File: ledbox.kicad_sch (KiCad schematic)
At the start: 0 parts

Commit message: Added XIAO
ledbox.kicad_pro: me changed 1 ERC rule severity; changed schematic
  settings.
ledbox.kicad_sch: me added U1 (XIAO-ESP32-C6-SMD).
pcbjam.lock.json: Library lockfile regenerated.

Checks: ERC: 19 errors in ledbox.kicad_sch (pin not connected ×18, power pin not driven ×1)

PCBJam-Commit: 692f007c-0890-4559-b9f4-d7b86e191ada
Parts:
- added U1: XIAO-ESP32-C6-SMD, Seeed_Studio_XIAO_Series:XIAO-ESP32-C6-SMD, symbol Seeed_Studio_XIAO_Series:XIAO-ESP32-C6-SMD
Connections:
- new net +3V3: U1.12 (3V3_OUT)
- new net +5V: U1.14 (VBUS)
- new net GND: U1.13 (GND), U1.24 (GND)
- no-connect marks 0 -> 2

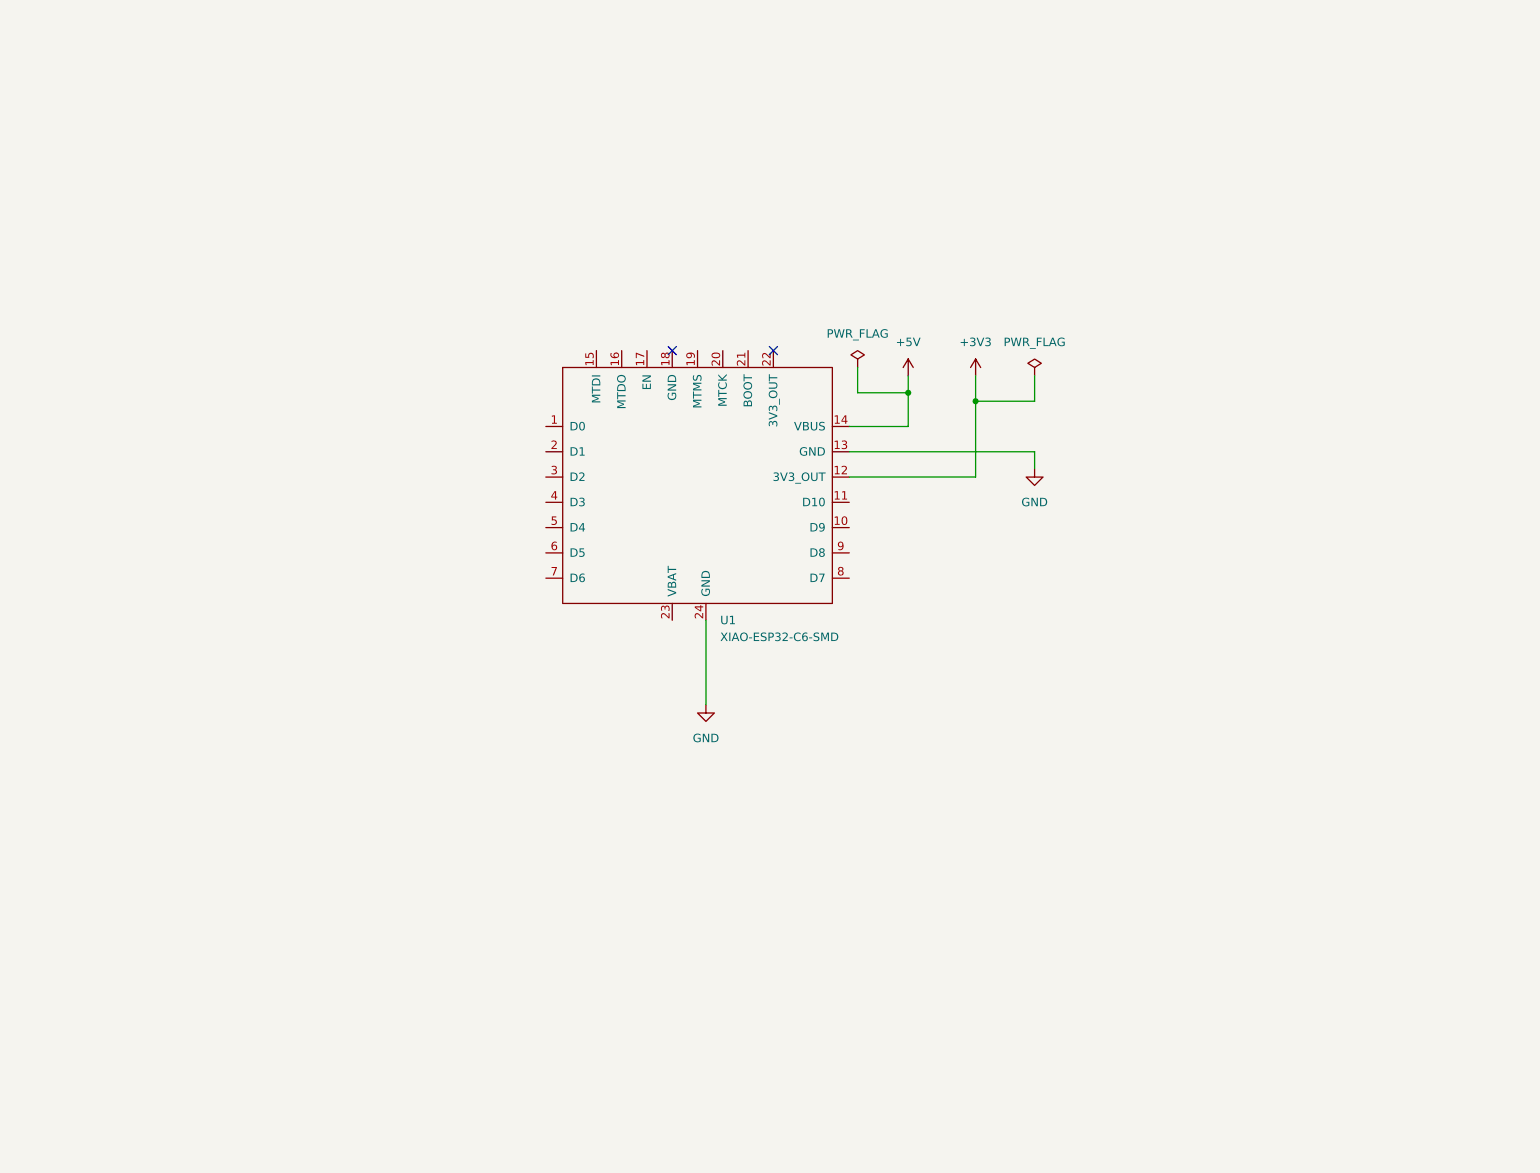
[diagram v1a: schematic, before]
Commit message: Finished Schematic.
ledbox.kicad_pro: me changed schematic settings.
ledbox.kicad_sch: me added D1, D2, J1-J8, SW1, SW2, TP1-TP4 and U2 and
  wired them; renamed net unconnected-(U1-D8-Pad9) to /A8; renamed net
  unconnected-(U1-D10-Pad11) to /STATUS_LED; rearranged the sheet around
  U1.
pcbjam.lock.json: Library lockfile regenerated.

Checks: ERC: 3 errors in ledbox.kicad_sch (pin not connected ×2, power pin not driven ×1)

PCBJam-Commit: e7df7650-f565-49c5-9b0e-8d383a5cb507
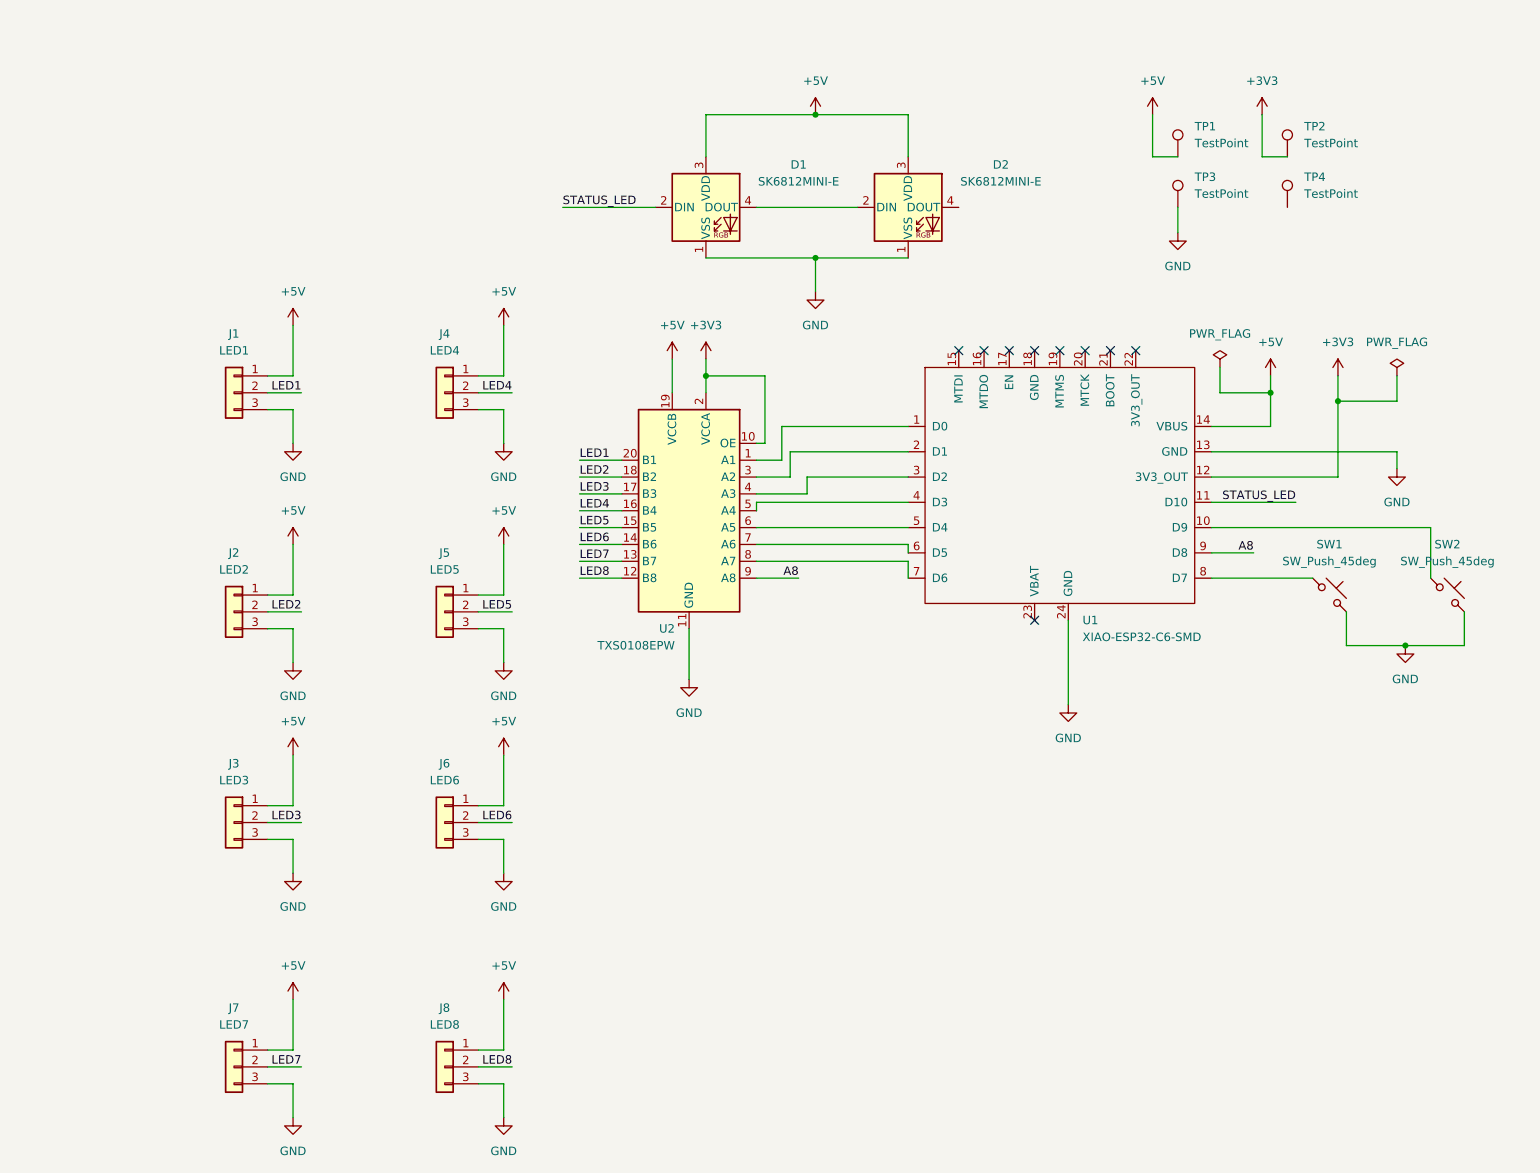
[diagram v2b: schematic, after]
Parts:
- added D1, D2: SK6812MINI-E, LED_SMD:LED_SK6812MINI-E_3.2x2.8mm_P1.5mm_ReverseMount, symbol LED:SK6812MINI-E
- added J1: LED1, symbol Connector_Generic:Conn_01x03
- added J2: LED2, symbol Connector_Generic:Conn_01x03
- added J3: LED3, symbol Connector_Generic:Conn_01x03
- added J4: LED4, symbol Connector_Generic:Conn_01x03
- added J5: LED5, symbol Connector_Generic:Conn_01x03
- added J6: LED6, symbol Connector_Generic:Conn_01x03
- added J7: LED7, symbol Connector_Generic:Conn_01x03
- added J8: LED8, symbol Connector_Generic:Conn_01x03
- added SW1, SW2: SW_Push_45deg, symbol Switch:SW_Push_45deg
- added TP1, TP2, TP3, TP4: TestPoint, TestPoint:TestPoint_Pad_D4.0mm, symbol Connector:TestPoint
- added U2: TXS0108EPW, Package_SO:TSSOP-20_4.4x6.5mm_P0.65mm, symbol Logic_LevelTranslator:TXS0108EPW
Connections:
- net +3V3: now also TP2.1, U2.10 (OE), U2.2 (VCCA)
- net +5V: now also D1.3 (VDD), D2.3 (VDD), J1.1 (Pin_1), J2.1 (Pin_1), J3.1 (Pin_1), J4.1 (Pin_1), J5.1 (Pin_1), J6.1 (Pin_1), J7.1 (Pin_1), J8.1 (Pin_1), TP1.1, U2.19 (VCCB)
- net GND: now also D1.1 (VSS), D2.1 (VSS), J1.3 (Pin_3), J2.3 (Pin_3), J3.3 (Pin_3), J4.3 (Pin_3), J5.3 (Pin_3), J6.3 (Pin_3), J7.3 (Pin_3), J8.3 (Pin_3), SW1.2, SW2.2, TP3.1, U2.11 (GND)
- net at U1.1 (D0): now also U2.1 (A1)
- net at U1.10 (D9): now also SW2.1
- net STATUS_LED: now reaches U1.11 (D10)
- net STATUS_LED: now also D1.2 (DIN)
- net at U1.2 (D1): now also U2.3 (A2)
- net at U1.3 (D2): now also U2.4 (A3)
- net at U1.4 (D3): now also U2.5 (A4)
- net at U1.5 (D4): now also U2.6 (A5)
- net at U1.6 (D5): now also U2.7 (A6)
- net at U1.7 (D6): now also U2.8 (A7)
- net at U1.8 (D7): now also SW1.1
- net A8: now reaches U1.9 (D8)
- net A8: now also U2.9 (A8)
- new net: D1.4 (DOUT), D2.2 (DIN)
- new net LED1: J1.2 (Pin_2), U2.20 (B1)
- new net LED2: J2.2 (Pin_2), U2.18 (B2)
- new net LED3: J3.2 (Pin_2), U2.17 (B3)
- new net LED4: J4.2 (Pin_2), U2.16 (B4)
- new net LED5: J5.2 (Pin_2), U2.15 (B5)
- new net LED6: J6.2 (Pin_2), U2.14 (B6)
- new net LED7: J7.2 (Pin_2), U2.13 (B7)
- new net LED8: J8.2 (Pin_2), U2.12 (B8)
- no-connect marks 2 -> 9
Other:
- moved on the sheet: U1

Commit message: add some footprint assignments
ledbox.kicad_sch: me changed 10 parts' fields; changed TP4 wiring (pin 1
  now on GND); rearranged the sheet.
pcbjam.lock.json: Library lockfile regenerated.

Checks: ERC: 2 errors in ledbox.kicad_sch (pin not connected ×1, power pin not driven ×1)

PCBJam-Commit: 97fe2138-5c53-4d5e-94ee-8a8dd15313f9
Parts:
- J1, J2, J3, J4, J5, J6, J7, J8: footprint (none) -> Connector_PinHeader_2.54mm:PinHeader_1x03_P2.54mm_Horizontal
- SW1, SW2: footprint (none) -> Button_Switch_SMD:SW_Push_1P1T_NO_CK_KMR2
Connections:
- net GND: now also TP4.1
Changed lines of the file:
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@@
 			)
 		)
-		(property "Footprint" ""
+		(property "Footprint" "Connector_PinHeader_2.54mm:PinHeader_1x03_P2.54mm_Horizontal"
 			(at 59.69 69.85 0)
 			(hide yes)
@@
 			)
 		)
-		(property "Footprint" ""
+		(property "Footprint" "Connector_PinHeader_2.54mm:PinHeader_1x03_P2.54mm_Horizontal"
 			(at 59.69 102.87 0)
 			(hide yes)
@@
 			)
 		)
-		(property "Footprint" ""
+		(property "Footprint" "Connector_PinHeader_2.54mm:PinHeader_1x03_P2.54mm_Horizontal"
 			(at 59.69 134.62 0)
 			(hide yes)
@@
 			)
 		)
-		(property "Footprint" ""
+		(property "Footprint" "Connector_PinHeader_2.54mm:PinHeader_1x03_P2.54mm_Horizontal"
 			(at 91.44 102.87 0)
 			(hide yes)
@@
 			)
 		)
-		(property "Footprint" ""
+		(property "Footprint" "Connector_PinHeader_2.54mm:PinHeader_1x03_P2.54mm_Horizontal"
 			(at 91.44 69.85 0)
 			(hide yes)
@@
 			)
 		)
-		(property "Footprint" ""
+		(property "Footprint" "Connector_PinHeader_2.54mm:PinHeader_1x03_P2.54mm_Horizontal"
 			(at 91.44 134.62 0)
 			(hide yes)
@@
 			)
 		)
-		(property "Footprint" ""
+		(property "Footprint" "Connector_PinHeader_2.54mm:PinHeader_1x03_P2.54mm_Horizontal"
 			(at 91.44 171.45 0)
 			(hide yes)
@@
 			)
 		)
-		(property "Footprint" ""
+		(property "Footprint" "Connector_PinHeader_2.54mm:PinHeader_1x03_P2.54mm_Horizontal"
 			(at 59.69 171.45 0)
 			(hide yes)
@@
 	(wire
 		(pts
-			(xy 201.93 45.72) (xy 201.93 41.91)
+			(xy 201.93 45.72) (xy 201.93 44.45)
 		)
 		(stroke
@@
 			)
 		)
-		(property "Footprint" ""
+		(property "Footprint" "Button_Switch_SMD:SW_Push_1P1T_NO_CK_KMR2"
 			(at 224.79 100.33 0)
 			(hide yes)
@@
 			)
 		)
-		(property "Footprint" ""
+		(property "Footprint" "Button_Switch_SMD:SW_Push_1P1T_NO_CK_KMR2"
 			(at 242.57 100.33 0)
 			(hide yes)
@@
 		)
 		(stroke
+			(width 0)
+			(type default)
+		)
+	)
+	(wire
+		(pts
+			(xy 218.44 44.45) (xy 201.93 44.45)
+		)
+		(stroke
+			(width 0)
+			(type default)
+		)
+	)
+	(junction
+		(at 201.93 44.45)
+		(diameter 0)
+		(color 0 0 0 0)
+	)
+	(wire
+		(pts
+			(xy 201.93 44.45) (xy 201.93 41.91)
+		)
+		(stroke
+			(width 0)
+			(type default)
+		)
+	)
+	(wire
+		(pts
+			(xy 218.44 41.91) (xy 218.44 44.45)
+		)
+		(stroke

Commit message: Assign xiao fooprint
ledbox.kicad_sch: me changed U1 footprint
  Seeed_Studio_XIAO_Series:XIAO-ESP32-C6-SMD → xiao:XIAO-ESP32-C6-SMD.
xiao.pretty/XIAO-ESP32-C6-SMD.kicad_mod: Added. me renamed the file.

Checks: ERC: 2 errors in ledbox.kicad_sch (pin not connected ×1, power pin not driven ×1)

PCBJam-Commit: 99d21ab3-7772-49a0-8721-84c00431a3ad
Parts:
- U1: footprint Seeed_Studio_XIAO_Series:XIAO-ESP32-C6-SMD -> xiao:XIAO-ESP32-C6-SMD
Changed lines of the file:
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@@
 			)
 		)
-		(property "Footprint" "Seeed_Studio_XIAO_Series:XIAO-ESP32-C6-SMD"
+		(property "Footprint" "xiao:XIAO-ESP32-C6-SMD"
 			(at 173.99 77.47 0)
 			(hide yes)

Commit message: i lowk forgot to commit in a while so ya
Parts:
- added U3: RPR-0521RS, Sensor:Rohm_RPR-0521RS, symbol Sensor:RPR-0521RS
- SW1, SW2: footprint Button_Switch_SMD:SW_Push_1P1T_NO_CK_KMR2 -> Button_Switch_SMD:SW_SPST_PTS645Sx43SMTR92
- TP1: value TestPoint -> +5V
- TP2: value TestPoint -> +3V3
- TP3: value TestPoint -> GND1
- TP4: value TestPoint -> GND2
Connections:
- net +3V3: now also U3.1 (VDD)
- net +5V: now also U3.4 (LED_A)
- net GND: now also U3.3 (GND)
- net A1: now reaches U1.1 (D0), U2.1 (A1)
- net A2: now reaches U1.2 (D1), U2.3 (A2)
- net A3: now reaches U1.3 (D2), U2.4 (A3)
- net A4: now reaches U1.4 (D3), U2.5 (A4)
- net A5: now reaches U2.6 (A5)
- net A5: now also U1.7 (D6); no longer U1.5 (D4)
- net A6: now reaches U2.7 (A6)
- net A6: now also U1.16 (MTDO); no longer U1.6 (D5)
- net A7: now reaches U2.8 (A7)
- net A7: now also U1.15 (MTDI); no longer U1.7 (D6)
- net INT: now reaches U1.19 (MTMS)
- net INT: now also U3.7 (INT)
- new net: U3.5 (LED_K), U3.6 (LDR)
- new net SCL: U1.6 (D5), U3.2 (SCL)
- new net SDA: U1.5 (D4), U3.8 (SDA)
- no-connect marks 9 -> 7
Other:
- moved on the sheet: J1, J2, J3, J4, J5, J6, J7, J8, U2
